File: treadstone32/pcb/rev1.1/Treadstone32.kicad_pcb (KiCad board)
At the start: 2 copper layers, 198.8 x 75.8 mm, 85 parts, among them J1 USB_mini_micro_B, J2 Conn_01x03, SW1 SW_PUSH, SW10 SW_PUSH, SW11 SW_PUSH, SW12 SW_PUSH, SW13 SW_PUSH, SW14 SW_PUSH, SW15 SW_PUSH, SW16 SW_PUSH, SW17 SW_PUSH, SW18 SW_PUSH, SW19 SW_PUSH, SW2 SW_PUSH, SW20 SW_PUSH, SW21 SW_PUSH, SW22 SW_PUSH, SW23 SW_PUSH, SW24 SW_PUSH, SW25 SW_PUSH, SW26 SW_PUSH, SW27 SW_PUSH, SW28 SW_PUSH, SW29 SW_PUSH, SW3 SW_PUSH, SW30 SW_PUSH, SW31 SW_PUSH, SW32 SW_PUSH, SW4 SW_PUSH, SW5 SW_PUSH, SW6 SW_PUSH, SW7 SW_PUSH, SW8 SW_PUSH, SW9 SW_PUSH, U1 ATMEGA32U4, X1 16MHz

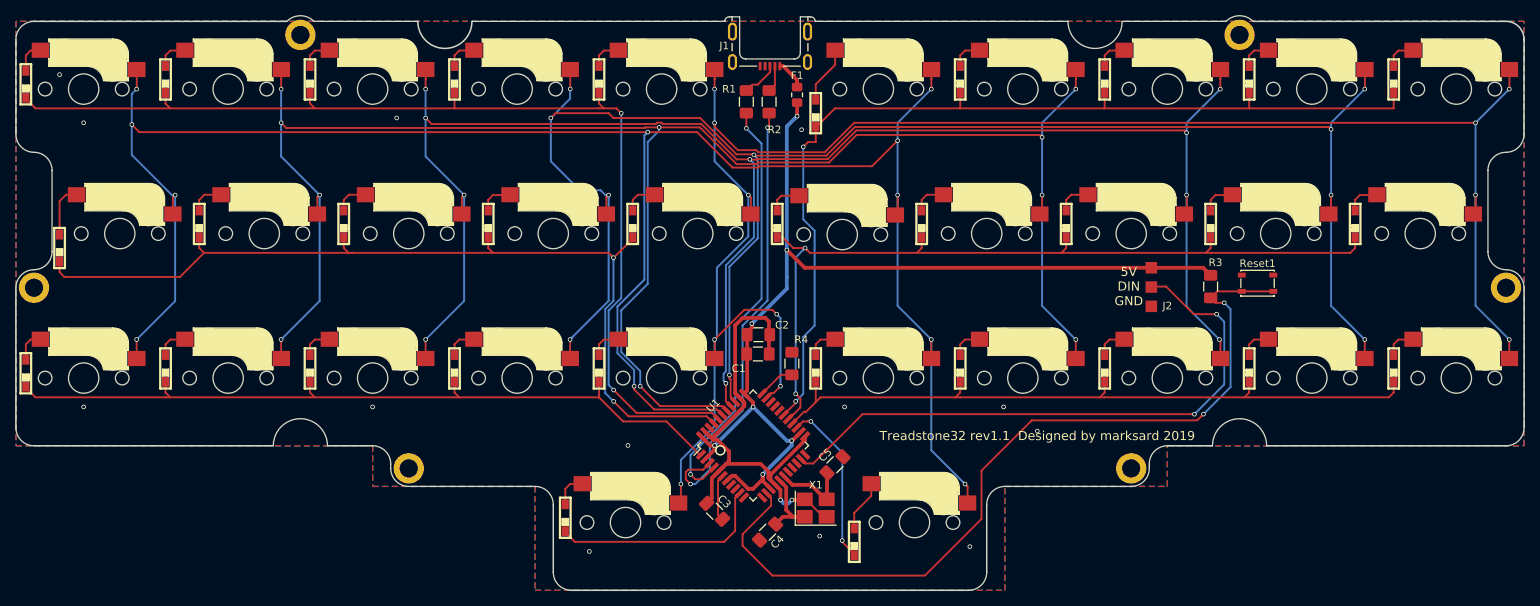
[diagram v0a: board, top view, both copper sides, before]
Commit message: Convert PCB to support USB type C connector
Added HRO Type C to replace J1 on schematic as well as C to C identifying resistors. Modified board edge cut and USB connector, re-routed data lines to new connector. Fixed issues with non-connecting polygons on edge cut.
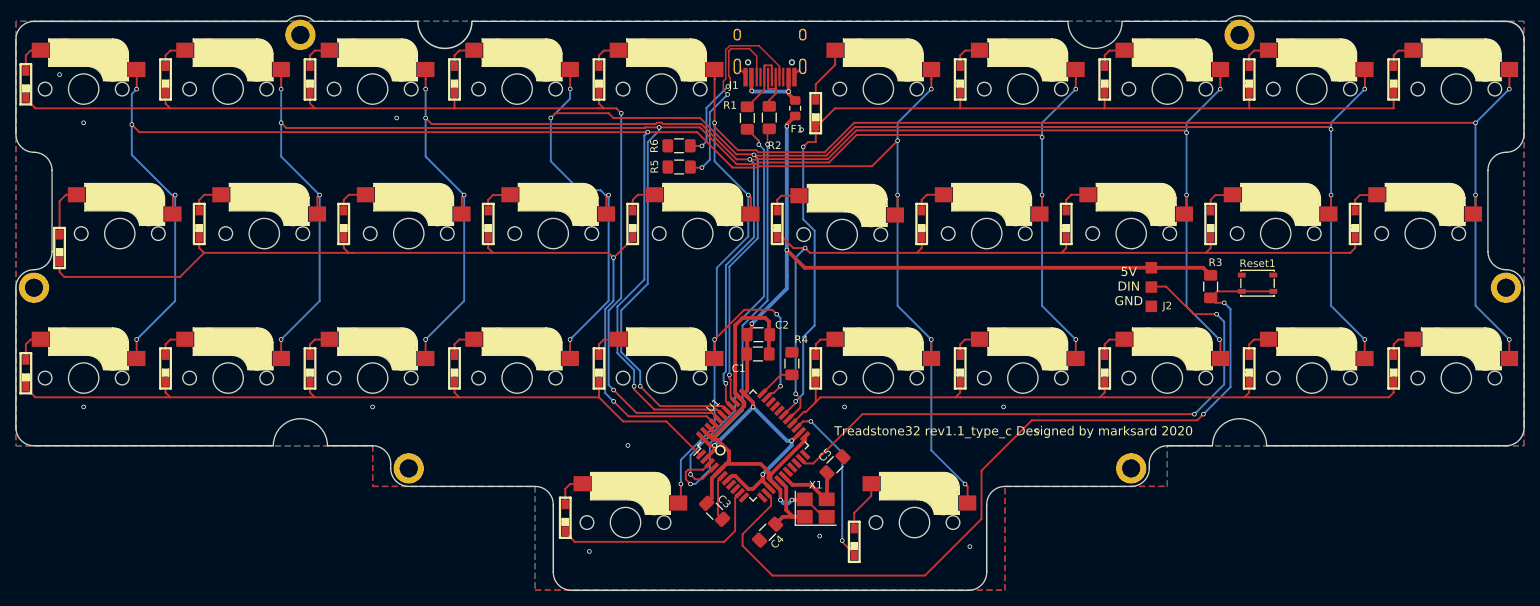
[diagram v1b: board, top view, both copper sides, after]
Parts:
- added R5: 5.1k, Resistor_SMD:R_1206_3216Metric_Pad1.42x1.75mm_HandSolder, F.Cu at (188.6, 77.5)
- added R6: 5.1k, Resistor_SMD:R_1206_3216Metric_Pad1.42x1.75mm_HandSolder, F.Cu at (188.6, 74.7)
- J1: value USB_mini_micro_B -> HRO-TYPE-C-31-M-12; footprint kbd:MOLEX_47642-0001_HandSoldering_cuts -> Type-C:HRO-TYPE-C-31-M-12-HandSoldering
- moved J1 4.00 mm to (200.6, 57.4)
- moved R1 2.14 mm to (197.6, 71.0)
- moved R2 2.08 mm to (200.5, 71.0)
- moved F1 1.78 mm to (203.9, 69.7)
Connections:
- J1 pad 1: Net-(F1-Pad1) -> GND
- J1 pad 2: Net-(J1-Pad2) -> Net-(F1-Pad1)
- J1 pad 4: (no net) -> CC1
- J1 pad 5: GND -> Net-(J1-Pad5)
- J1 pad 6: GND -> Net-(J1-Pad6)
- R1 pad 1: Net-(J1-Pad3) -> Net-(J1-Pad6)
- R2 pad 1: Net-(J1-Pad2) -> Net-(J1-Pad5)
- U1 pad 11: (no net) -> Net-(U1-Pad11)
- U1 pad 12: (no net) -> Net-(U1-Pad12)
- U1 pad 18: (no net) -> Net-(U1-Pad18)
- U1 pad 19: (no net) -> Net-(U1-Pad19)
- U1 pad 20: (no net) -> Net-(U1-Pad20)
- U1 pad 22: (no net) -> Net-(U1-Pad22)
- U1 pad 29: (no net) -> Net-(U1-Pad29)
- U1 pad 30: (no net) -> Net-(U1-Pad30)
- U1 pad 31: (no net) -> Net-(U1-Pad31)
- U1 pad 42: (no net) -> Net-(U1-Pad42)
- U1 pad 8: (no net) -> Net-(U1-Pad8)
- U1 pad 9: (no net) -> Net-(U1-Pad9)
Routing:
- net CC1: track 0.00 -> 28.7 mm, vias 0 -> 2
- net CC2: track 0.00 -> 22.7 mm, vias 0 -> 2
- net Net-(J1-Pad6): track 0.00 -> 8.84 mm
- net Net-(J1-Pad5): track 0.00 -> 6.75 mm
- net Net-(F1-Pad1): track 3.96 -> 10.3 mm, vias 0 -> 2
- net Net-(J1-Pad3): track 4.92 -> 0.00 mm
- net GND: track 66.1 -> 69.9 mm
- net Net-(J1-Pad2): track 3.53 -> 0.00 mm
- net VCC: track 136.5 -> 134.6 mm
- net Net-(R1-Pad2): track 56.3 -> 54.7 mm
- net Net-(R2-Pad2): track 59.0 -> 57.6 mm
- net col4: vias 11 -> 10
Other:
- outline, holes or cut-outs redrawn
- board text added: "Treadstone32 rev1.1_type_c Designed by marksard 2020"
- board text removed: "Treadstone32 rev1.1 Designed by marksard 2019"
